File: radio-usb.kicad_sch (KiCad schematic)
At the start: 233 parts, among them J1 Barrel_Jack, J10 Conn_Coaxial, J11 ACJS-MHDRM, J12 ACJS-MHDRM, J2 miniUSB, J3 15EDGRC-3.5-03P-14, J4 DB9_Female, J5 EEP_EN, J6 Mini-DIN-6, J7 EDAC 690-008-221-904, J8 DB9_Male, J9 Conn_Coaxial, Q1 BC846C, Q2 BC846C, Q3 BC846C, Q4 BC846C, Q5 BC856, SW1 SW_Push_DPDT, SW2 SW_SPDT, SW3 SW_SPDT, SW4 SW_DIP_x04, SW5 SW_DIP_x04, SW6 SW_DPDT_x2, SW7 SW_SPDT, U1 L7805, U10 AP2171W, U11 TLP2662, U12 TLP2662, U13 MAX3232, U14 93CxxC, U15 PCM2900CDB, U17 FT2232HL, U18 PC817, U19 CRIYCHLEY9000, U2 24LC04, U20 PC817, U21 PC817, U22 CRIYCHLEY9000, U23 LMV321IDBVR, U3 APX809_810-xxSA, U4 AP22814AW5, U5 AP22814AW5, U6 USB2514B-AEZC, U7 LM1117-3.3, U8 TBA 1-0511, U9 4069, X1 MAB5SH, Y1 24MHz, Y2 12MHz, Y3 12M

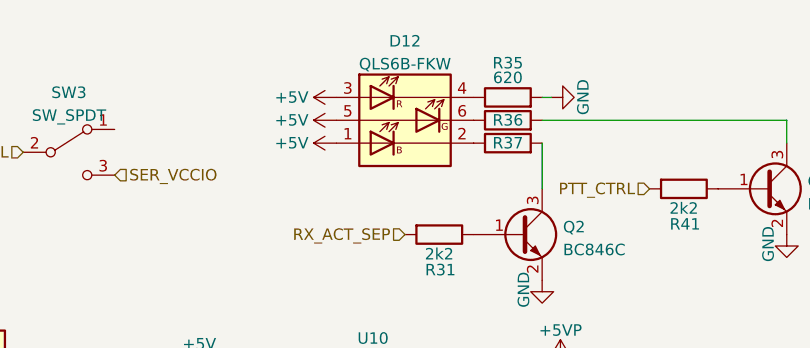
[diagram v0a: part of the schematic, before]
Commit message: updated bom and exported schematic, corrected some component values
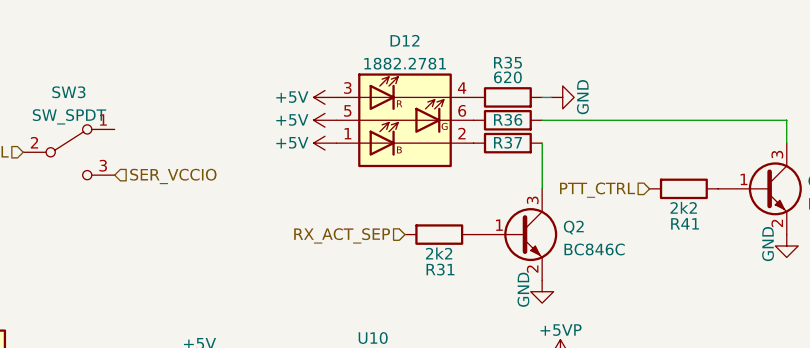
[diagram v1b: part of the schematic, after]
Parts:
- D12: value QLS6B-FKW -> 1882.2781
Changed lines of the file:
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@@
     (in_bom yes) (on_board yes) (fields_autoplaced)
     (property "Reference" "D12" (id 0) (at 167.64 15.3502 0))
-    (property "Value" "QLS6B-FKW" (id 1) (at 167.64 17.8871 0))
+    (property "Value" "1882.2781" (id 1) (at 167.64 17.8871 0))
     (property "Footprint" "LED:LED_MENTOR_1882" (id 2) (at 162.56 32.258 0)
       (effects (font (size 1.27 1.27)) (justify left) hide)
@@
     )
     (path "/deb0672d-1fa7-4c50-aa33-536d20962dc3"
-      (reference "D12") (unit 1) (value "QLS6B-FKW") (footprint "LED:LED_MENTOR_1882")
+      (reference "D12") (unit 1) (value "1882.2781") (footprint "LED:LED_MENTOR_1882")
     )
     (path "/b2315279-acc3-4d1c-ac73-aa85b2d0ceeb"

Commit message: gerber exports and another files sent to PCBway for production
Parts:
- removed Y1: 24MHz, Crystal:Crystal_SMD_Abracon_ABM8G-4Pin_3.2x2.5mm, symbol Device:Crystal_Small
- removed Y2: 12MHz, Crystal:Crystal_SMD_Abracon_ABM8G-4Pin_3.2x2.5mm, symbol Device:Crystal
- removed Y3: 12M, Crystal:Crystal_SMD_Abracon_ABM8G-4Pin_3.2x2.5mm, symbol Device:Crystal
- added Y1: 24MHz, Crystal:Crystal_SMD_Abracon_ABM8G-4Pin_3.2x2.5mm, symbol Device:Crystal_GND24
- added Y2, Y3: 12MHz, Crystal:Crystal_SMD_Abracon_ABM8G-4Pin_3.2x2.5mm, symbol Device:Crystal_GND24
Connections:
- net GND: now also Y1.4, Y2.1, Y3.4
- net H_XTALIN: now also Y1.1
- net H_XTALO: now also Y1.3
- net SER_XI: now also Y2.2
- net SER_XO: now also Y2.4
- net at C52.1, R55.1, U15.20 (XTO): now also Y3.1
- net at C51.1, R55.2, U15.21 (XTI): now also Y3.3
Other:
- moved on the sheet: C2, C30, C31, C5

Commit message: fix with Y1 part number, cleanup in output files
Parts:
- Y1: DESCRIPTION LFXTAL032817BULK -> 24.00M-SMDXT324 YIC
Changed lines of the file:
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@@
       (effects (font (size 1.27 1.27)) hide)
     )
-    (property "DESCRIPTION" "LFXTAL032817BULK" (id 4) (at 45.212 91.694 0)
+    (property "DESCRIPTION" "24.00M-SMDXT324  YIC" (id 4) (at 45.212 91.694 0)
       (effects (font (size 1.27 1.27)) hide)
     )

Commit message: more cleanup
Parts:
- SW4, SW5: value SW_DIP_x04 -> A6H-4101; DESCRIPTION NIDEC CHS-04B -> OMRON A6H-4101
- U14: value 93CxxC -> AT93C46D
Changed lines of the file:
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@@
     (in_bom yes) (on_board yes) (fields_autoplaced)
     (property "Reference" "SW5" (id 0) (at 350.012 106.5362 0))
-    (property "Value" "SW_DIP_x04" (id 1) (at 350.012 109.0731 0))
+    (property "Value" "A6H-4101" (id 1) (at 350.012 109.0731 0))
     (property "Footprint" "Button_Switch_SMD:SW_DIP_SPSTx04_Slide_Copal_CHS-04B_W7.62mm_P1.27mm" (id 2) (at 350.012 117.856 0)
       (effects (font (size 1.27 1.27)) hide)
@@
       (effects (font (size 1.27 1.27)) hide)
     )
-    (property "DESCRIPTION" "NIDEC CHS-04B" (id 4) (at 350.012 117.856 0)
+    (property "DESCRIPTION" "OMRON A6H-4101" (id 4) (at 350.012 117.856 0)
       (effects (font (size 1.27 1.27)) hide)
     )
@@
   )
   (symbol (lib_id "Memory_EEPROM:93CxxC") (at 231.648 106.426 0) (unit 1)
-    (in_bom yes) (on_board yes) (fields_autoplaced)
-    (property "Reference" "U14" (id 0) (at 233.6674 97.6462 0)
+    (in_bom yes) (on_board yes)
+    (property "Reference" "U14" (id 0) (at 221.996 96.774 0)
       (effects (font (size 1.27 1.27)) (justify left))
     )
-    (property "Value" "93CxxC" (id 1) (at 233.6674 100.1831 0)
+    (property "Value" "AT93C46D" (id 1) (at 221.996 98.552 0)
       (effects (font (size 1.27 1.27)) (justify left))
     )
@@
     (in_bom yes) (on_board yes) (fields_autoplaced)
     (property "Reference" "SW4" (id 0) (at 345.186 56.4982 0))
-    (property "Value" "SW_DIP_x04" (id 1) (at 345.186 59.0351 0))
+    (property "Value" "A6H-4101" (id 1) (at 345.186 59.0351 0))
     (property "Footprint" "Button_Switch_SMD:SW_DIP_SPSTx04_Slide_Copal_CHS-04B_W7.62mm_P1.27mm" (id 2) (at 345.186 67.818 0)
       (effects (font (size 1.27 1.27)) hide)
@@
       (effects (font (size 1.27 1.27)) hide)
     )
-    (property "DESCRIPTION" "NIDEC CHS-04B" (id 4) (at 345.186 67.818 0)
+    (property "DESCRIPTION" "OMRON A6H-4101" (id 4) (at 345.186 67.818 0)
       (effects (font (size 1.27 1.27)) hide)
     )
@@
     )
     (path "/f55bfe01-b74b-486a-8b14-abb298385552"
-      (reference "SW4") (unit 1) (value "SW_DIP_x04") (footprint "Button_Switch_SMD:SW_DIP_SPSTx04_Slide_Copal_CHS-04B_W7.62mm_P1.27mm")
+      (reference "SW4") (unit 1) (value "A6H-4101") (footprint "Button_Switch_SMD:SW_DIP_SPSTx04_Slide_Copal_CHS-04B_W7.62mm_P1.27mm")
     )
     (path "/26ceab95-3188-4c91-b949-b084811f8200"
-      (reference "SW5") (unit 1) (value "SW_DIP_x04") (footprint "Button_Switch_SMD:SW_DIP_SPSTx04_Slide_Copal_CHS-04B_W7.62mm_P1.27mm")
+      (reference "SW5") (unit 1) (value "A6H-4101") (footprint "Button_Switch_SMD:SW_DIP_SPSTx04_Slide_Copal_CHS-04B_W7.62mm_P1.27mm")
     )
     (path "/1a7ebf5b-ec79-4dfb-82d6-6de9c8f2a745"
@@
     )
     (path "/bfe8c080-0416-4f15-bdd7-c77de414263c"
-      (reference "U14") (unit 1) (value "93CxxC") (footprint "Package_DIP:DIP-8_W7.62mm")
+      (reference "U14") (unit 1) (value "AT93C46D") (footprint "Package_DIP:DIP-8_W7.62mm")
     )
     (path "/307d7eea-37f5-408d-8df4-29d797cc6b8b"

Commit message: hardware revision b schematic
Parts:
- removed D10, D9: RB751V40T1G, Diode_SMD:D_SOD-323_HandSoldering, symbol Diode:1N6857
- removed R21: 100k, Resistor_SMD:R_0805_2012Metric_Pad1.20x1.40mm_HandSolder, symbol Device:R
- added SW?: SW_SPDT, switches_spdt_dpdt:Alps_SSSS213000, symbol Switch:SW_SPDT
- added U?: 74AHCT1G04, symbol 74xGxx:74AHCT1G04
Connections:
- net GND: now also U?.3 (GND)
- net PTT_CTRL: now also SW3.3 (C), U?.2; no longer R63.1, SW3.2 (B)
- net SER_B_RXD_IN: now also SW?.2 (B)
- net at R25.1, U11.6 (VO2): now also SW?.1 (A)
- net at R29.1, U11.7 (VO1): now also SW?.3 (C)
- net at R63.2: now also SW3.2 (B); no longer Q4.1 (B)
- net ~{PTT_CTRL}: now reaches SW3.1 (A)
- net ~{PTT_CTRL}: now also U?.4
- net SER_VCCIO renamed VCC
- net VCC: now also U?.5 (VCC); no longer SW3.3 (C)
- new net PTT_CTRL_SW: Q4.1 (B), R63.1
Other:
- moved on the sheet: D12, Q2, Q3, R31, R35, R36, R37, R41, R63, SW3

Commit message: daily
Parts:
- removed R64, R71, R72, R77: 10k, Resistor_SMD:R_0805_2012Metric_Pad1.20x1.40mm_HandSolder, symbol Device:R
- removed TP12: OPAMP_BIAS, TestPoint:TestPoint_Pad_D2.0mm, symbol Connector:TestPoint
- removed U23: LMV321IDBVR, Package_TO_SOT_SMD:SOT-23-5_HandSoldering, symbol Amplifier_Operational:LMV321
- SW8: renamed from SW?; footprint switches_spdt_dpdt:Alps_SSSS213000 -> switches_spdt_dpdt:Ninigi_MSS-2235S
- U16: renamed from U?; footprint (none) -> Package_TO_SOT_SMD:SOT-23-5_HandSoldering
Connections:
- net at C62.1: now also R67.2, R68.2
- net at R25.1, U11.6 (VO2): now also SW8.3 (C); no longer SW8.1 (A)
- net at R29.1, U11.7 (VO1): now also SW8.1 (A); no longer SW8.3 (C)
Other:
- moved on the sheet: C62

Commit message: hw revision b done
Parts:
- removed R25: 2k2, Resistor_SMD:R_0805_2012Metric_Pad1.20x1.40mm_HandSolder, symbol Device:R
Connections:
- net SER_B_RXD_IN: now also R29.1
- net SER_B_RXD_TTL: now reaches SW8.1 (A), U11.7 (VO1)
- net SER_B_RXD_TTL: no longer R29.1
- net SER_B_RXD_RS: now reaches SW8.3 (C), U11.6 (VO2)
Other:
- moved on the sheet: R29, SW8

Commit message: hardware revision b build
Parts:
- D5: value LED_HS -> DNP
- J8: symbol Connector:DB9_Male -> Connector:DB9_Male_MountingHoles
- R1: value 100k -> DNP
- R3: value 620 -> DNP
- R7: value 10k -> DNP
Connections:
- net +3V3: now also R57.1, R59.1
- net GND: now also Y2.2; no longer R57.1, R59.1, Y2.1
- net GNDREF: now also J8.0 (PAD)
- net SER_B_RXLED: now also D16.1 (K); no longer D16.2 (A)
- net SER_B_TXLED: now also D15.1 (K); no longer D15.2 (A)
- net SER_XI: now also Y2.3; no longer Y2.2
- net SER_XO: now also Y2.1; no longer Y2.4
- net at R59.2: now also D16.2 (A); no longer D16.1 (K)
- net at R57.2: now also D15.2 (A); no longer D15.1 (K)
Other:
- moved on the sheet: D15, D16, Y2
